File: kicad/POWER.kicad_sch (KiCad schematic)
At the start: 54 parts, among them U1 AP2127K-ADJTRG1, U2 MT9700, U3 SY8892ARC, U4 AP2127K-ADJTRG1, U5 SY8892ARC, U6 SY8892ARC

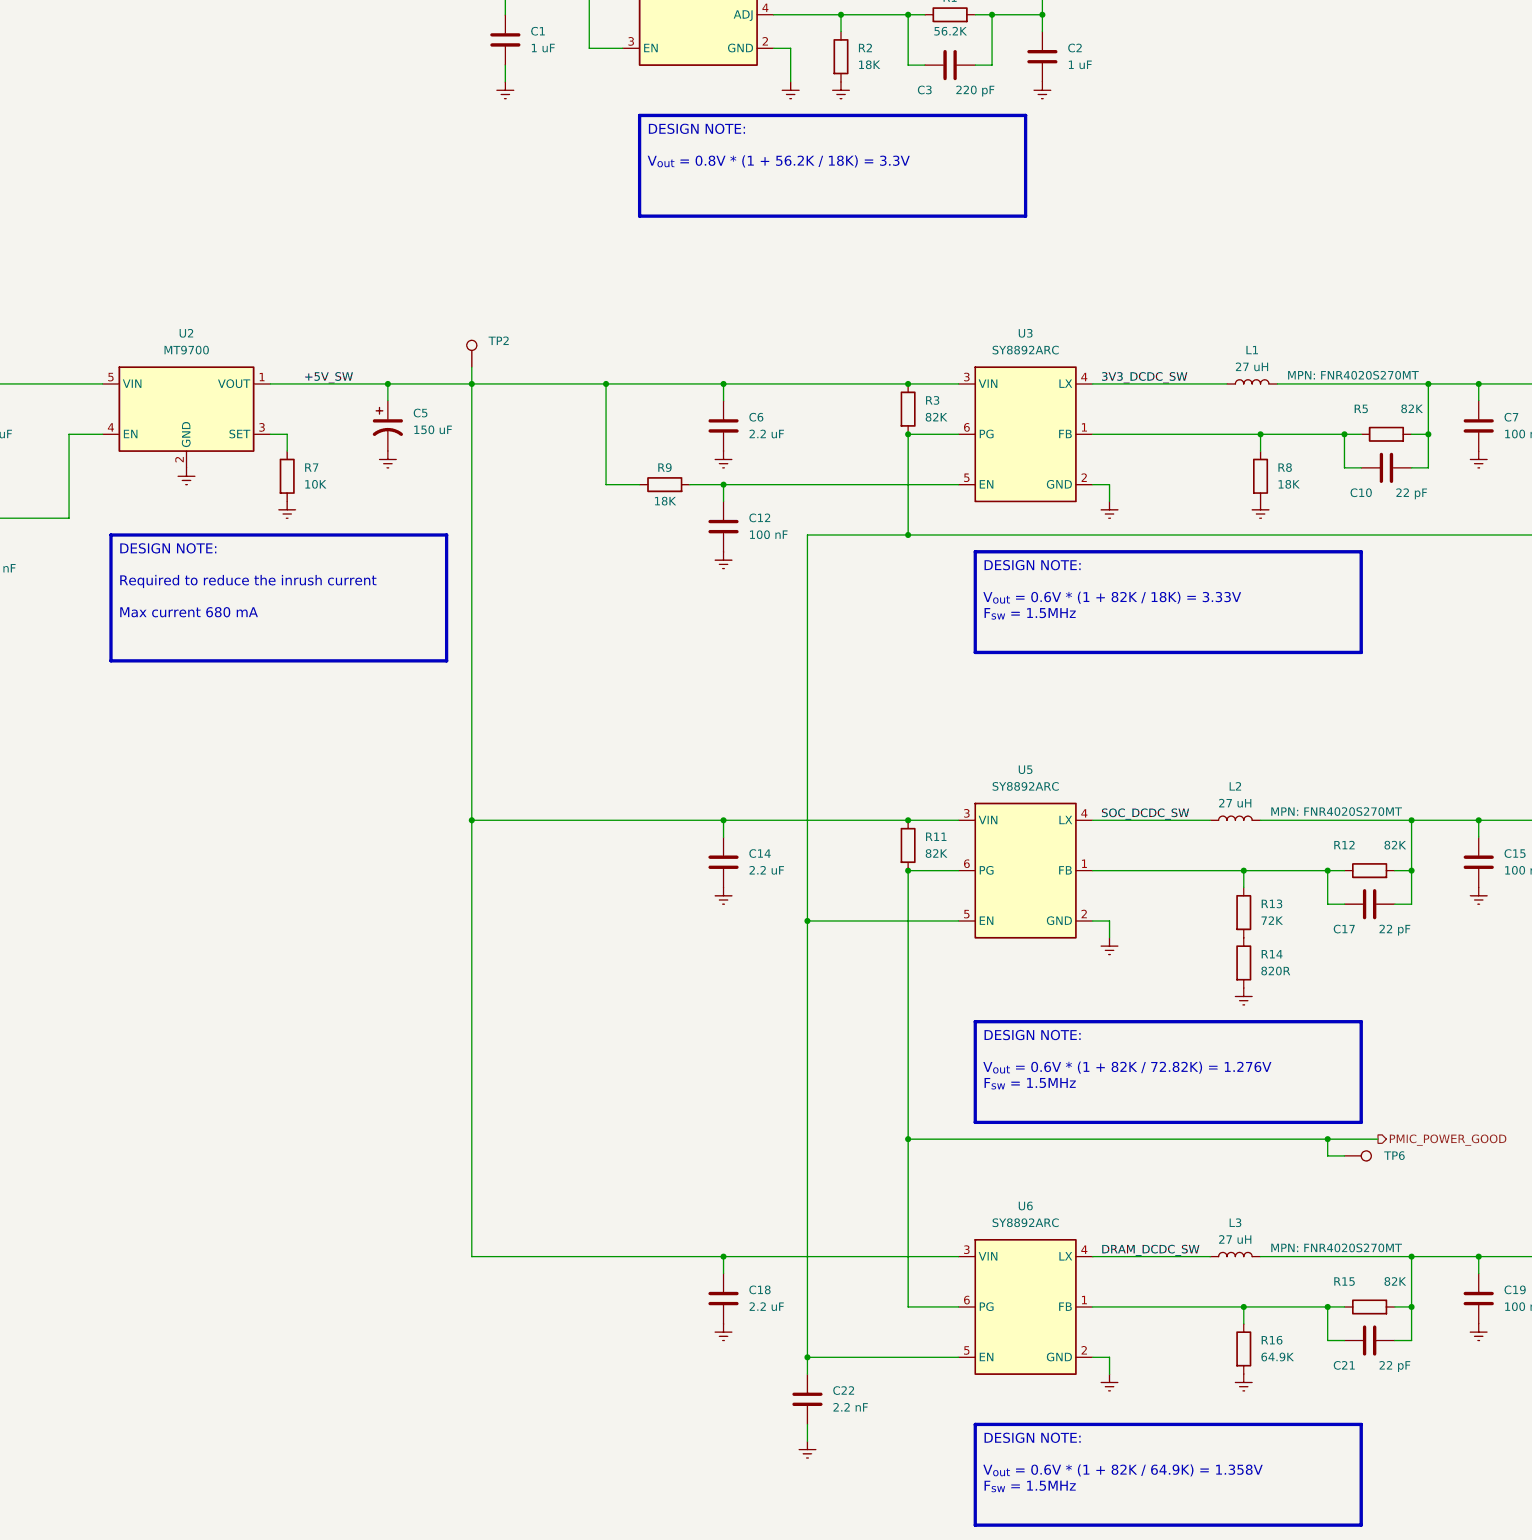
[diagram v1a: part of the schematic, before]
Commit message: Fix hardware bugs - Fix part number in bom for resistors R103, R113, R114, R118 -> 680K - Fix part number in BOM for resistors R13, R16 -> 68K - Fix part number in BOM for resistor R14 -> 4.7K - Fix part number in BOM for capacitors C100, C101, C12, C13, C130, C131, C133, C135, C140, C141, C15, C19, C57, C58, C7, C99 -> 100nF - Fix footprint for USB-A connectors - Fix power buttom pull-up resistor connection -> connect to +3.3V_STAND_BY
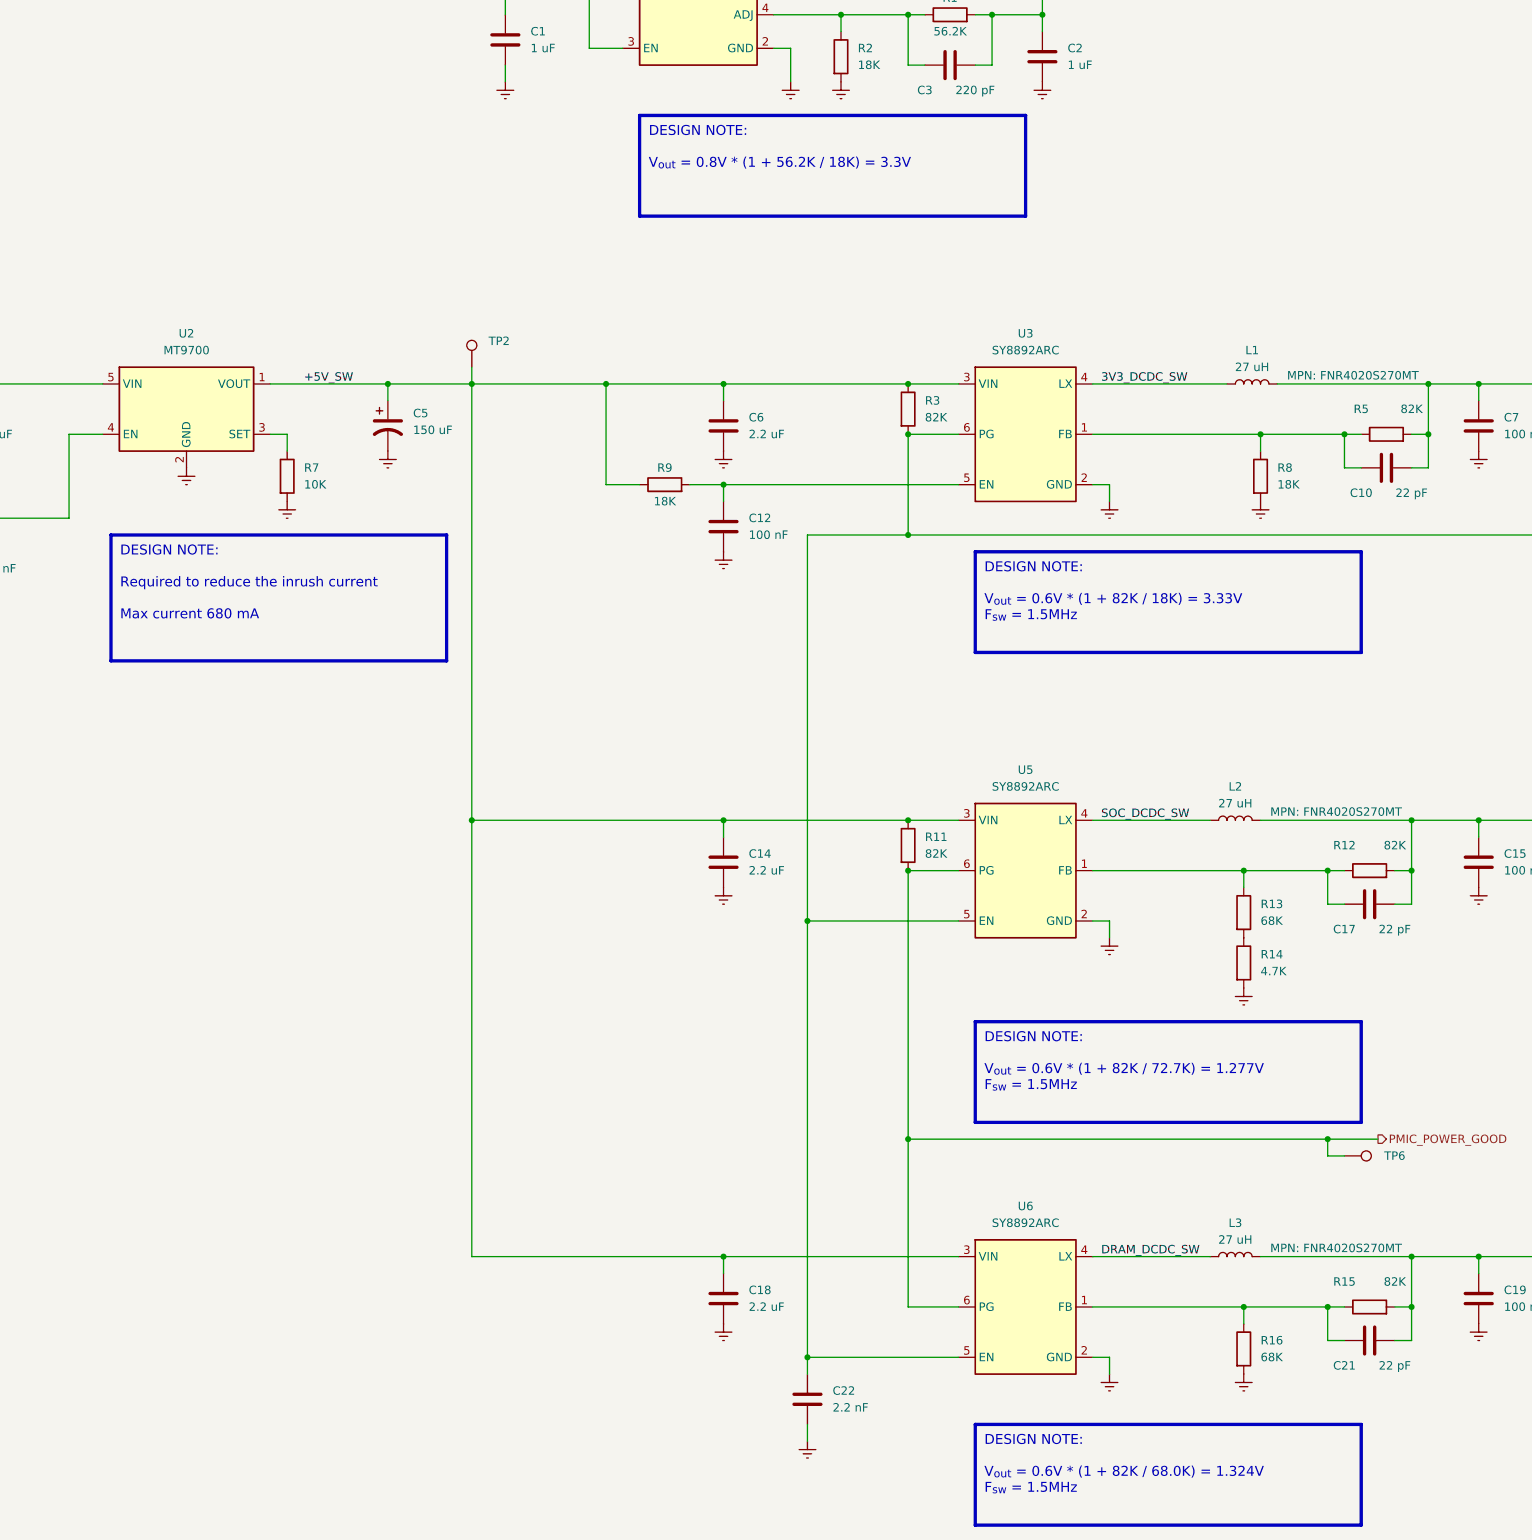
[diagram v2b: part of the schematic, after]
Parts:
- C12, C13, C15, C19, C7: symbol -- database:Capacitors/CAP_0402-100n-50V-X7R-10% -> ts_database:Capacitors/CAP_0402-100n-50V-X7R-10%; LCSC C1523 -> C77020
- R13: value 72K -> 68K; symbol -- database:Resistors/RES-SMD-0402-72K-1/16W-1% -> ts_database:Resistors/RES-SMD-0402-68K-1/16W-1%; LCSC C852446 -> C36871; Mouser 603-RC0402FR-0772KL -> 603-RC0402FR-0768KL
- R14: value 820R -> 4.7K; symbol -- database:Resistors/RES-SMD-0402-820R-1/16W-1% -> ts_database:Resistors/RES-SMD-0402-4K7-1/16W-1%; LCSC C431726 -> C105871; Mouser 603-RC0402FR-0718KL -> 603-RC0402FR-074K7L
- R16: value 64.9K -> 68K; symbol -- database:Resistors/RES-SMD-0402-64K9-1/16W-1% -> ts_database:Resistors/RES-SMD-0402-68K-1/16W-1%; LCSC C3016024 -> C36871; Mouser 603-RC0402FR-0764K9L -> 603-RC0402FR-0768KL
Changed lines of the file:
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@@
 (kicad_sch
-	(version 20231120)
+	(version 20250114)
 	(generator "eeschema")
-	(generator_version "8.0")
+	(generator_version "9.0")
 	(paper "A3")
 	(title_block
 		(title "i.MX6 Demo Board")
-		(date "2024-05-26")
-		(rev "00")
+		(date "2026-02-16")
+		(rev "01")
 		(company "ts-manuel")
 	)
+	(text_box "DESIGN NOTE:\n\nV_{out} = 0.6V * (1 + 82K / 72.7K) = 1.277V\nF_{sw} = 1.5MHz"
+		(exclude_from_sim no)
+		(at 198.12 200.66 0)
+		(size 58.42 15.24)
+		(margins 1.375 1.375 1.375 1.375)
+		(stroke
+			(width 0.5)
+			(type solid)
+			(color 255 229 153 1)
+		)
+		(fill
+			(type color)
+			(color 243 243 243 1)
+		)
+		(effects
+			(font
+				(size 1.5 1.5)
+			)
+			(justify left top)
+		)
+	)
+	(text_box "DESIGN NOTE:\n\nV_{out} = 0.8V * (1 + 56.2K / 18K) = 3.3V"
+		(exclude_from_sim no)
+		(at 147.32 63.5 0)
+		(size 58.42 15.24)
+		(margins 1.375 1.375 1.375 1.375)
+		(stroke
+			(width 0.5)
+			(type default)
+			(color 255 229 153 1)
+		)
+		(fill
+			(type color)
+			(color 243 243 243 1)
+		)
+		(effects
+			(font
+				(size 1.5 1.5)
+			)
+			(justify left top)
+		)
+	)
+	(text_box "DESIGN NOTE:\n\nV_{out} = 0.6V * (1 + 82K / 68.0K) = 1.324V\nF_{sw} = 1.5MHz"
+		(exclude_from_sim no)
+		(at 198.12 261.62 0)
+		(size 58.42 15.24)
+		(margins 1.375 1.375 1.375 1.375)
+		(stroke
+			(width 0.5)
+			(type solid)
+			(color 255 229 153 1)
+		)
+		(fill
+			(type color)
+			(color 243 243 243 1)
+		)
+		(effects
+			(font
+				(size 1.5 1.5)
+			)
+			(justify left top)
+		)
+	)
+	(text_box "DESIGN NOTE:\n\nV_{out} = 0.6V * (1 + 82K / 18K) = 3.33V\nF_{sw} = 1.5MHz"
+		(exclude_from_sim no)
+		(at 198.12 129.54 0)
+		(size 58.42 15.24)
+		(margins 1.375 1.375 1.375 1.375)
+		(stroke
+			(width 0.5)
+			(type default)
+			(color 255 229 153 1)
+		)
+		(fill
+			(type color)
+			(color 243 243 243 1)
+		)
+		(effects
+			(font
+				(size 1.5 1.5)
+			)
+			(justify left top)
+		)
+	)
+	(text_box "DESIGN NOTE:\n\nRequired to reduce the inrush current\n\nMax current 680 mA"
+		(exclude_from_sim no)
+		(at 67.31 127 0)
+		(size 50.8 19.05)
+		(margins 1.375 1.375 1.375 1.375)
+		(stroke
+			(width 0.5)
+			(type default)
+			(color 255 229 153 1)
+		)
+		(fill
+			(type color)
+			(color 243 243 243 1)
+		)
+		(effects
+			(font
+				(size 1.5 1.5)
+			)
+			(justify left top)
+		)
+	)
 	(junction
 		(at 187.96 177.8)
@@
 		)
 	)
-	(text_box "DESIGN NOTE:\n\nV_{out} = 0.6V * (1 + 82K / 72.82K) = 1.276V\nF_{sw} = 1.5MHz"
-		(exclude_from_sim no)
-		(at 198.12 200.66 0)
-		(size 58.42 15.24)
-		(stroke
-			(width 0.5)
-			(type default)
-			(color 255 229 153 1)
-		)
-		(fill
-			(type color)
-			(color 243 243 243 1)
-		)
-		(effects
-			(font
-				(size 1.5 1.5)
-			)
-			(justify left top)
-		)
-	)
-	(text_box "DESIGN NOTE:\n\nV_{out} = 0.8V * (1 + 56.2K / 18K) = 3.3V"
-		(exclude_from_sim no)
-		(at 147.32 63.5 0)
-		(size 58.42 15.24)
-		(stroke
-			(width 0.5)
-			(type default)
-			(color 255 229 153 1)
-		)
-		(fill
-			(type color)
-			(color 243 243 243 1)
-		)
-		(effects
-			(font
-				(size 1.5 1.5)
-			)
-			(justify left top)
-		)
-	)
-	(text_box "DESIGN NOTE:\n\nV_{out} = 0.6V * (1 + 82K / 64.9K) = 1.358V\nF_{sw} = 1.5MHz"
-		(exclude_from_sim no)
-		(at 198.12 261.62 0)
-		(size 58.42 15.24)
-		(stroke
-			(width 0.5)
-			(type default)
-			(color 255 229 153 1)
-		)
-		(fill
-			(type color)
-			(color 243 243 243 1)
-		)
-		(effects
-			(font
-				(size 1.5 1.5)
-			)
-			(justify left top)
-		)
-	)
-	(text_box "DESIGN NOTE:\n\nV_{out} = 0.6V * (1 + 82K / 18K) = 3.33V\nF_{sw} = 1.5MHz"
-		(exclude_from_sim no)
-		(at 198.12 129.54 0)
-		(size 58.42 15.24)
-		(stroke
-			(width 0.5)
-			(type default)
-			(color 255 229 153 1)
-		)
-		(fill
-			(type color)
-			(color 243 243 243 1)
-		)
-		(effects
-			(font
-				(size 1.5 1.5)
-			)
-			(justify left top)
-		)
-	)
-	(text_box "DESIGN NOTE:\n\nRequired to reduce the inrush current\n\nMax current 680 mA"
-		(exclude_from_sim no)
-		(at 67.31 127 0)
-		(size 50.8 19.05)
-		(stroke
-			(width 0.5)
-			(type default)
-			(color 255 229 153 1)
-		)
-		(fill
-			(type color)
-			(color 243 243 243 1)
-		)
-		(effects
-			(font
-				(size 1.5 1.5)
-			)
-			(justify left top)
-		)
-	)
 	(label "3V3_DCDC_SW"
 		(at 217.17 104.14 0)
-		(fields_autoplaced yes)
 		(effects
 			(font
@@
 	(label "SOC_DCDC_SW"
 		(at 217.17 170.18 0)
-		(fields_autoplaced yes)
 		(effects
 			(font
@@
 	(label "DRAM_DCDC_SW"
 		(at 217.17 236.22 0)
-		(fields_autoplaced yes)
 		(effects
 			(font
@@
 	(label "+5V_SW"
 		(at 96.52 104.14 0)
-		(fields_autoplaced yes)
 		(effects
 			(font
@@
 		(shape input)
 		(at 30.48 124.46 180)
-		(fields_autoplaced yes)
 		(effects
 			(font
@@
 		(shape output)
 		(at 259.08 218.44 0)
-		(fields_autoplaced yes)
 		(effects
 			(font
@@
 	)
 	(symbol
-		(lib_id "-- database:Capacitors/CAP_0402-100n-50V-X7R-10%")
+		(lib_id "ts_database:Capacitors/CAP_0402-100n-50V-X7R-10%")
 		(at 274.32 110.49 0)
 		(unit 1)
@@
 			)
 		)
-		(property "LCSC" "C1523"
+		(property "LCSC" "C77020"
 			(at 274.32 110.49 0)
 			(show_name yes)
@@
 	)
 	(symbol
-		(lib_id "-- database:Resistors/RES-SMD-0402-72K-1/16W-1%")
+		(lib_id "ts_database:Resistors/RES-SMD-0402-68K-1/16W-1%")
 		(at 238.76 184.15 0)
 		(unit 1)
@@
 			)
 		)
-		(property "Value" "72K"
+		(property "Value" "68K"
 			(at 241.3 185.4199 0)
 			(effects
@@
 			)
 		)
-		(property "Description" "Thick Film Resistor - SMD 0402 72K 1% 1/16W"
+		(property "Description" "Thick Film Resistor - SMD 0402 68K 1% 1/16W"
 			(at 238.76 184.15 0)
 			(effects
@@
 			)
 		)
-		(property "Mouser" "603-RC0402FR-0772KL"
+		(property "Mouser" "603-RC0402FR-0768KL"
 			(at 238.76 184.15 0)
 			(show_name yes)
@@
 			)
 		)
-		(property "LCSC" "C852446"
+		(property "LCSC" "C36871"
 			(at 238.76 184.15 0)
 			(show_name yes)
@@
 	)
 	(symbol
-		(lib_id "-- database:Capacitors/CAP_0402-100n-50V-X7R-10%")
+		(lib_id "ts_database:Capacitors/CAP_0402-100n-50V-X7R-10%")
 		(at 274.32 242.57 0)
 		(unit 1)
@@
 			)
 		)
-		(property "LCSC" "C1523"
+		(property "LCSC" "C77020"
 			(at 274.32 242.57 0)
 			(show_name yes)
@@
 	)
 	(symbol
-		(lib_id "-- database:Resistors/RES-SMD-0402-820R-1/16W-1%")
+		(lib_id "ts_database:Resistors/RES-SMD-0402-4K7-1/16W-1%")
 		(at 238.76 191.77 0)
 		(unit 1)
@@
 			)
 		)
-		(property "Value" "820R"
+		(property "Value" "4.7K"
 			(at 241.3 193.0399 0)
 			(effects
@@
 			)
 		)
-		(property "Description" "Thick Film Resistor - SMD 0402 820R 1% 1/16W"
+		(property "Description" "Thick Film Resistor - SMD 0402 4.7K 1% 1/16W"
 			(at 238.76 191.77 0)
 			(effects
@@
 			)
 		)
-		(property "Mouser" "603-RC0402FR-0718KL"
+		(property "Mouser" "603-RC0402FR-074K7L"
 			(at 238.76 191.77 0)
 			(show_name yes)
@@
 			)
 		)
-		(property "LCSC" "C431726"
+		(property "LCSC" "C105871"
 			(at 238.76 191.77 0)
 			(show_name yes)
@@
 	)
 	(symbol
-		(lib_id "-- database:Capacitors/CAP_0402-100n-50V-X7R-10%")
+		(lib_id "ts_database:Capacitors/CAP_0402-100n-50V-X7R-10%")
 		(at 274.32 176.53 0)
 		(unit 1)
@@
 			)
 		)
-		(property "LCSC" "C1523"
+		(property "LCSC" "C77020"
 			(at 274.32 176.53 0)
 			(show_name yes)
@@
 	)
 	(symbol
-		(lib_id "-- database:Resistors/RES-SMD-0402-64K9-1/16W-1%")
+		(lib_id "ts_database:Resistors/RES-SMD-0402-68K-1/16W-1%")
 		(at 238.76 250.19 0)
 		(unit 1)
@@
 			)
 		)
-		(property "Value" "64.9K"
+		(property "Value" "68K"
 			(at 241.3 251.4599 0)
 			(effects
@@
 			)
 		)
-		(property "Description" "Thick Film Resistor - SMD 0402 64.9K 1% 1/16W"
+		(property "Description" "Thick Film Resistor - SMD 0402 68K 1% 1/16W"
 			(at 238.76 250.19 0)
 			(effects
@@
 			)
 		)
-		(property "Mouser" "603-RC0402FR-0764K9L"
+		(property "Mouser" "603-RC0402FR-0768KL"
 			(at 238.76 250.19 0)
 			(show_name yes)
@@
 			)
 		)
-		(property "LCSC" "C3016024"
+		(property "LCSC" "C36871"
 			(at 238.76 250.19 0)
 			(show_name yes)
@@
 	)
 	(symbol
-		(lib_id "-- database:Capacitors/CAP_0402-100n-50V-X7R-10%")
+		(lib_id "ts_database:Capacitors/CAP_0402-100n-50V-X7R-10%")
 		(at 160.02 125.73 0)
 		(unit 1)
@@
 			)
 		)
-		(property "LCSC" "C1523"
+		(property "LCSC" "C77020"
 			(at 160.02 125.73 0)
 			(show_name yes)
@@
 	)
 	(symbol
-		(lib_id "-- database:Capacitors/CAP_0402-100n-50V-X7R-10%")
+		(lib_id "ts_database:Capacitors/CAP_0402-100n-50V-X7R-10%")
 		(at 43.18 130.81 0)
 		(unit 1)
@@
 			)
 		)
-		(property "LCSC" "C1523"
+		(property "LCSC" "C77020"
 			(at 43.18 130.81 0)
 			(show_name yes)
